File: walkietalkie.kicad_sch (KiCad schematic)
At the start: 7 parts, among them SW2 SW_Push, U2 NRF24L01_Breakout

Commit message: schematics done
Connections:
- net +3.3V: now also 1.VCC, Brd1.2 (VCC), U2.2 (VCC), U4.1 (3.3V)
- net SCL: now reaches Brd1.3 (SCL), U1.1 (SCL)
- net SCL: now also U3.5 (SCL)
- net BAT: now reaches U1.12 (BAT)
- net BAT: now also U3.1 (5V)
- net at U1.14 (3V3): no longer Brd1.2 (VCC)
- net GND: now reaches Brd1.1 (GND), U2.1 (GND)
- net GND: now also 1.GND, SW2.2, U1.28 (GND), U3.3 (G), U4.2 (GND); no longer U1.16 (GND)
- net CE: now reaches U1.17 (D13)
- net CE: now also U2.3 (CE)
- net CSN: now reaches U1.18 (D14)
- net CSN: now also U2.4 (~{CSN})
- net SDA: now reaches Brd1.4 (SDA), U1.2 (SDA)
- net SDA: now also U3.4 (SDA)
- net MIC_SD: now reaches U1.20 (D16)
- net MIC_SD: now also U4.5 (SD)
- net LRCK: now reaches U1.21 (D17)
- net LRCK: now also U3.9 (LRCK), U4.3 (WS)
- net BCLK: now reaches U1.22 (D18)
- net BCLK: now also U3.7 (BCK), U4.4 (SCK)
- net SCK: now reaches U1.23 (SCK)
- net SCK: now also U2.5 (SCK)
- net MO: now reaches U1.24 (MO)
- net MO: now also U2.6 (MOSI)
- net MI: now reaches U1.25 (MI)
- net MI: now also U2.7 (MISO)
- net ENC_SW: now reaches U1.4 (A2)
- net ENC_SW: now also 1.SW
- net NAU_MCLK: now reaches U1.5 (A6)
- net NAU_MCLK: now also U3.6 (MCLK)
- net NAU_DAT: now reaches U1.6 (A7)
- net NAU_DAT: now also U3.8 (DAT)
- net ENC_A: now reaches U1.7 (A8)
- net ENC_A: now also 1.CLK
- net PTT: now reaches U1.8 (A9)
- net PTT: now also SW2.1
- net ENC_B: now reaches U1.9 (A10)
- net ENC_B: now also 1.DT
- new net +3V3: U1.15 (3V3)
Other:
- moved on the sheet: 1, Brd1, U1, U3, U4

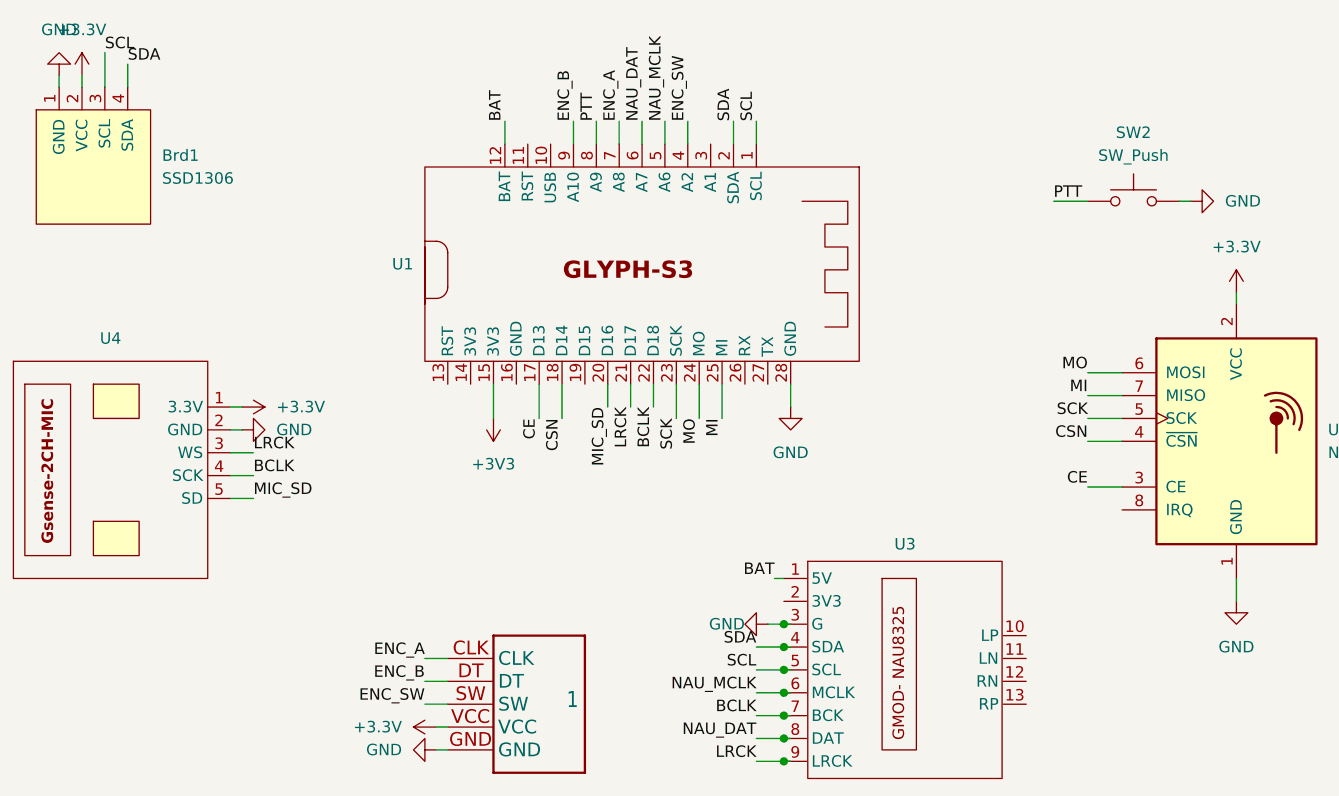
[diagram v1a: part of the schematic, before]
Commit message: assigning footprints done
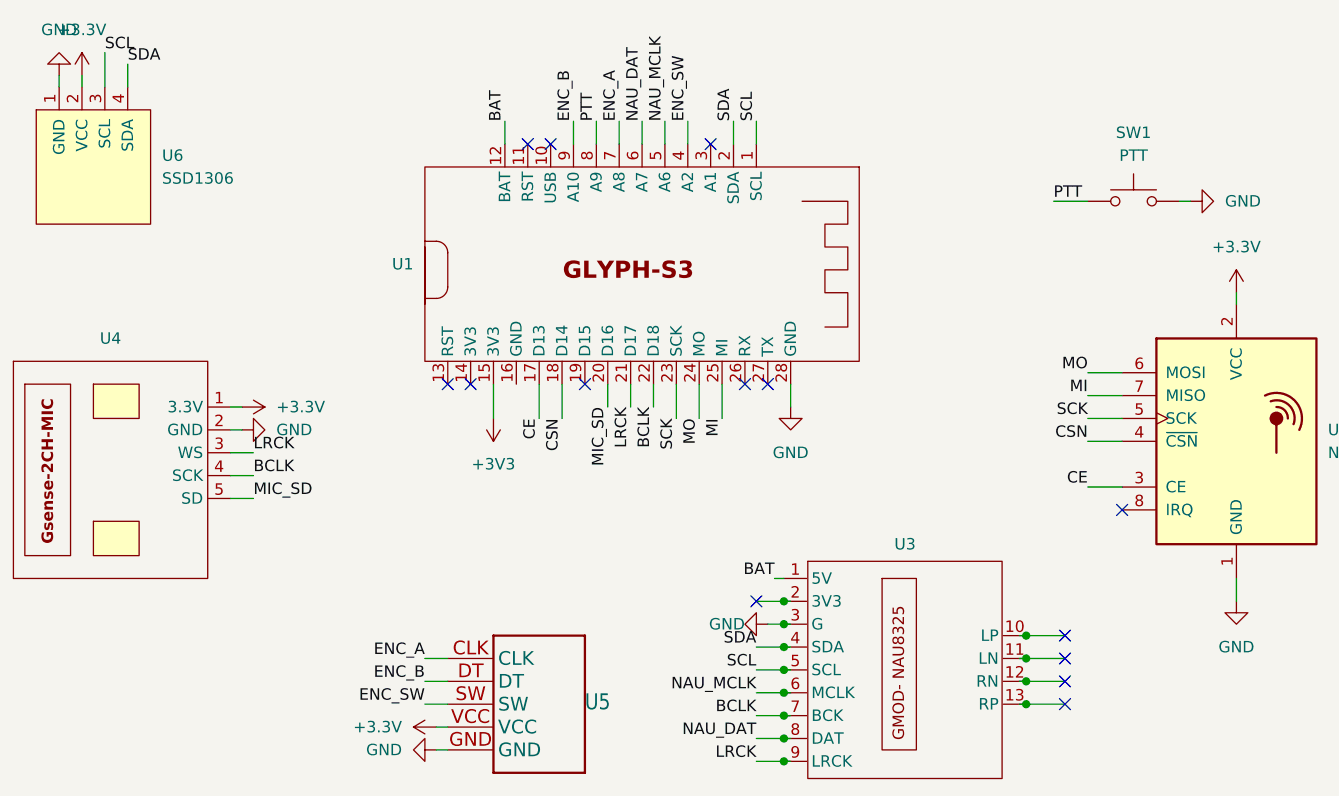
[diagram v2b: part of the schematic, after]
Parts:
- SW1: renamed from SW2; value SW_Push -> PTT; footprint (none) -> Button_Switch_THT:SW_SPST_Omron_B3F-315x_Angled
- U1: footprint GLYPHC6:GLYPH-C6 -> pcbcupid_footprint:glyph-s3
- U3: footprint Audiocodec_foot:Audio_codec -> pcbcupid_footprint:gmod-audio_codec
- U4: footprint (none) -> pcbcupid_footprint:gsense-microphone_2ch
- U5: renamed from 1; footprint KY-040:KY-040-PORT -> kicadfoots:KY-040-PORT
- U6: renamed from Brd1; footprint (none) -> kicadfoots:128x64OLED
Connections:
- no-connect marks 0 -> 14

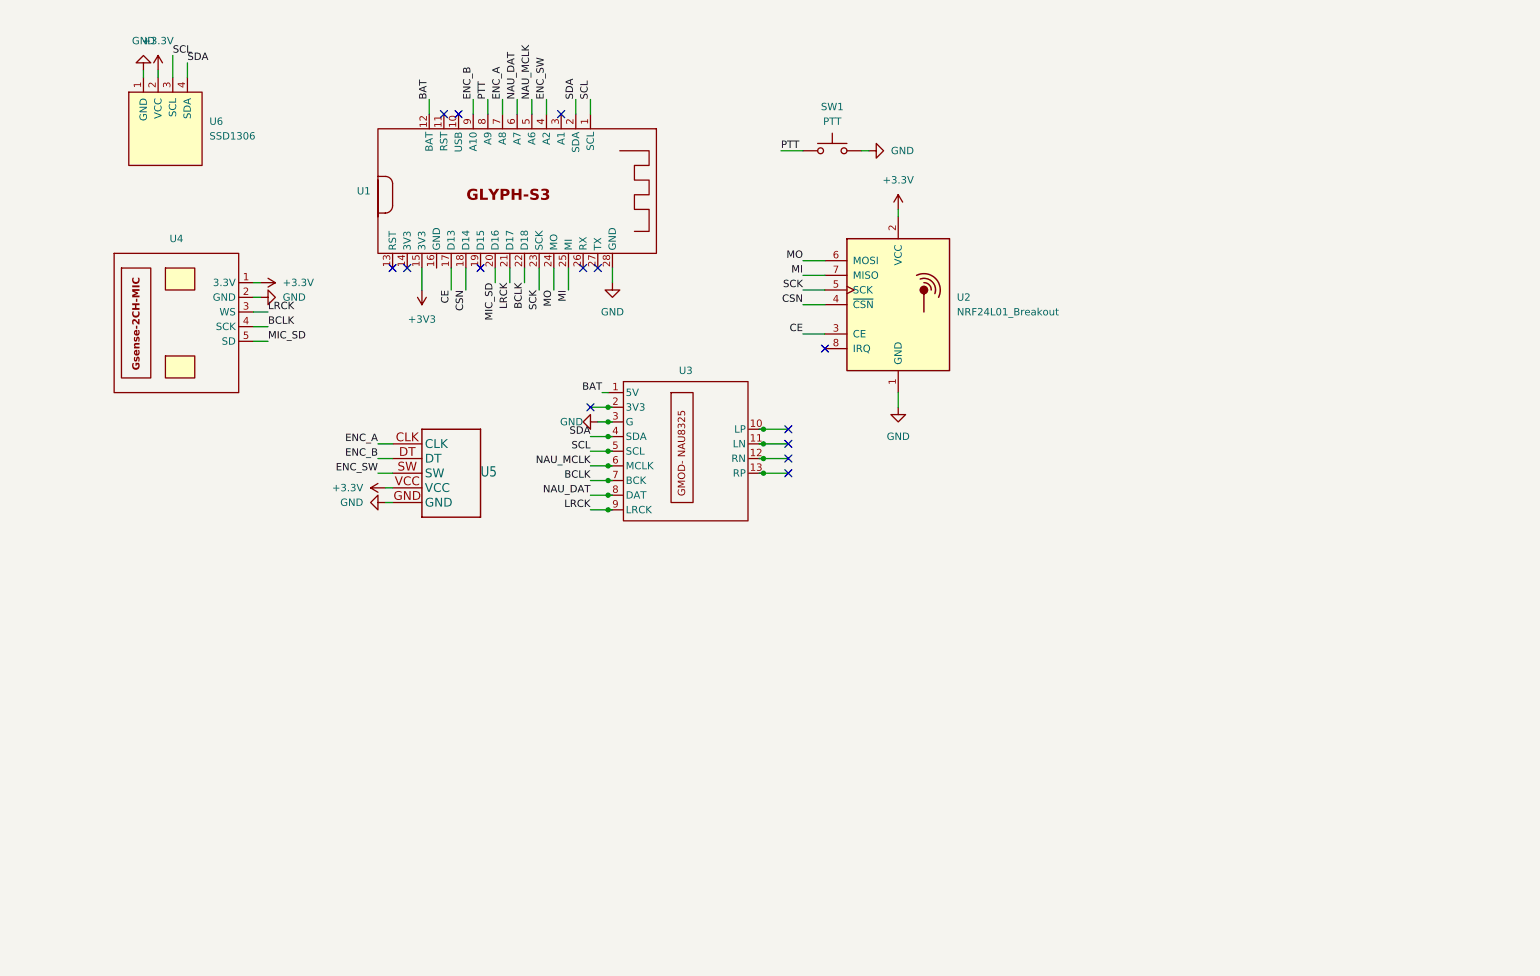
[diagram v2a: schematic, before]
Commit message: placements of the components are done, routing left
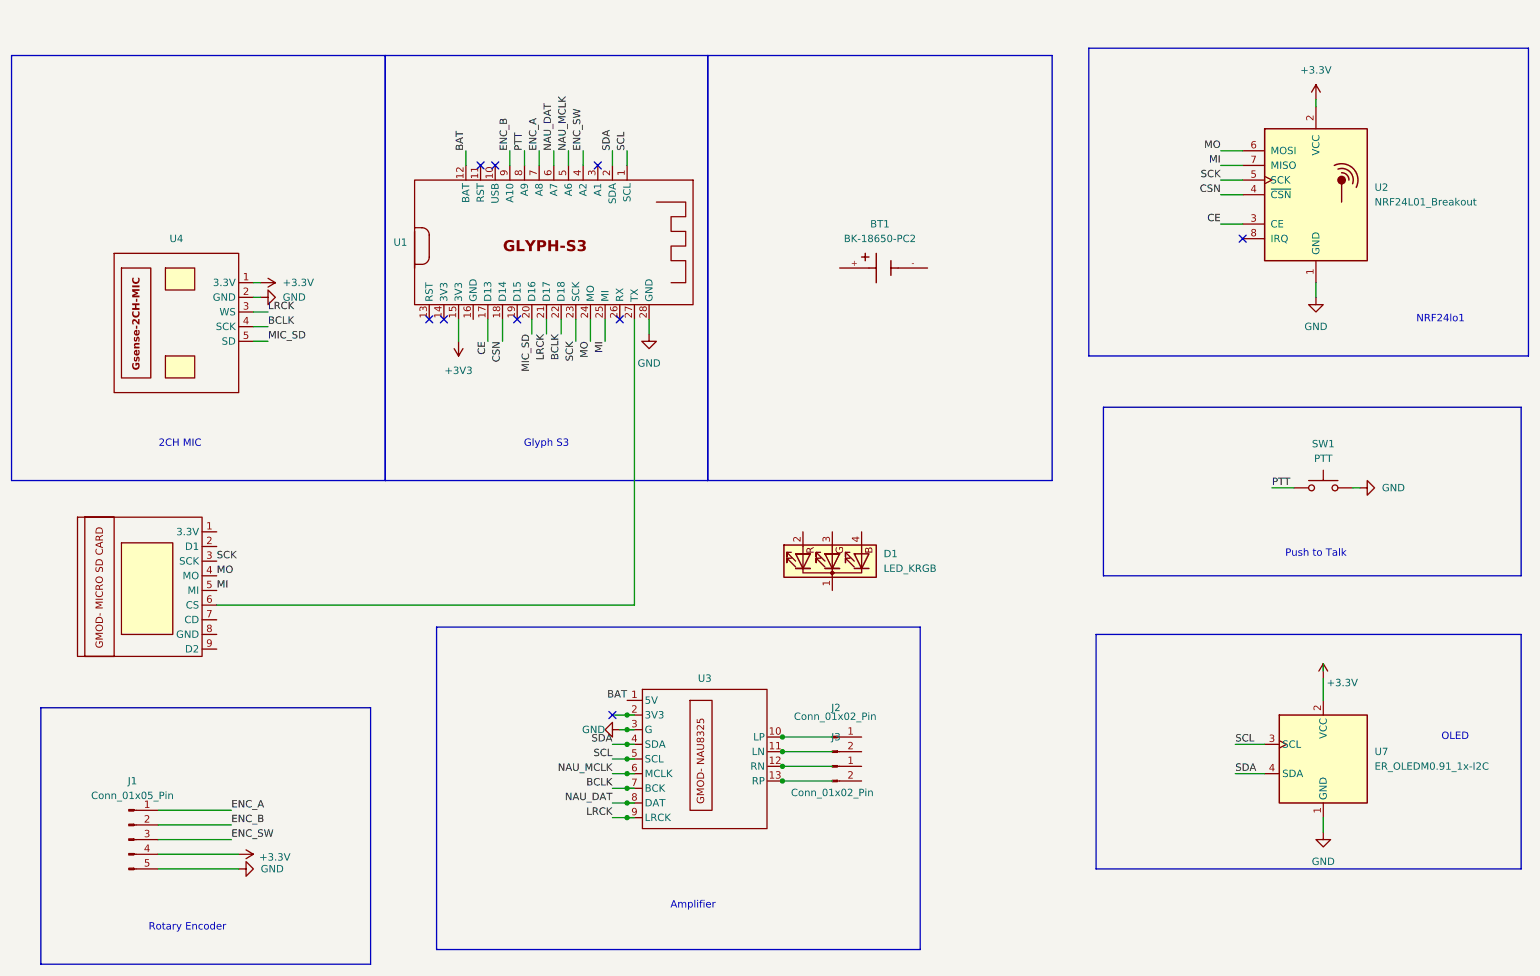
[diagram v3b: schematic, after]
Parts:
- removed U5: (no value), kicadfoots:KY-040-PORT, symbol KY-040:KY-040
- removed U6: SSD1306, kicadfoots:128x64OLED, symbol SSD1306-128x64_OLED:SSD1306
- added BT1: BK-18650-PC2, pcbcupid_footprint:BAT_BK-18650-PC2, symbol single:BK-18650-PC2
- added D1: LED_KRGB, symbol Device:LED_KRGB
- added J1: Conn_01x05_Pin, Connector_PinHeader_1.27mm:PinHeader_1x05_P1.27mm_Horizontal, symbol Connector:Conn_01x05_Pin
- added J2, J3: Conn_01x02_Pin, symbol Connector:Conn_01x02_Pin
- added U5: (no value), pcbcupid_footprint:gmod-micro_sd, symbol single:GMOD- MICRO SD CARD
- added U7: ER_OLEDM0.91_1x-I2C, Display:ER_OLEDM0.91_1x-I2C, symbol Display_Graphic:ER_OLEDM0.91_1x-I2C
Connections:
- net +3.3V: now also J1.4 (Pin_4), U7.2 (VCC)
- net ENC_A: now also J1.1 (Pin_1)
- net ENC_B: now also J1.2 (Pin_2)
- net ENC_SW: now also J1.3 (Pin_3)
- net GND: now also J1.5 (Pin_5), U7.1 (GND)
- net MI: now also U5.5 (MI)
- net MO: now also U5.4 (MO)
- net SCK: now also U5.3 (SCK)
- net SCL: now also U7.3 (SCL)
- net SDA: now also U7.4 (SDA)
- net at U1.27 (TX): now also U5.6 (CS)
- no-connect marks 14 -> 9
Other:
- note added: "2CH MIC"
- note added: "Amplifier"
- note added: "Glyph S3"
- note added: "NRF24lo1"
- note added: "OLED"
- note added: "Push to Talk"
- note added: "Rotary Encoder"
- company: (none) -> PCB CUPID
- title: (none) -> TeleVox
- moved on the sheet: SW1, U1, U2, U3

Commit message: feat: finalize component placement, routing remaining
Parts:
- BT1: footprint pcbcupid_footprint:BAT_BK-18650-PC2 -> pcbcupidd_footprint:BatteryHolder_1042_1x18650
- D1: footprint (none) -> LED_THT:LED_D5.0mm-4_RGB
- J1: footprint Connector_PinHeader_1.27mm:PinHeader_1x05_P1.27mm_Horizontal -> Connector_PinHeader_2.54mm:PinHeader_1x05_P2.54mm_Vertical
- J2, J3: footprint (none) -> Connector_JST:JST_XH_S2B-XH-A_1x02_P2.50mm_Horizontal
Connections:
- no-connect marks 9 -> 12

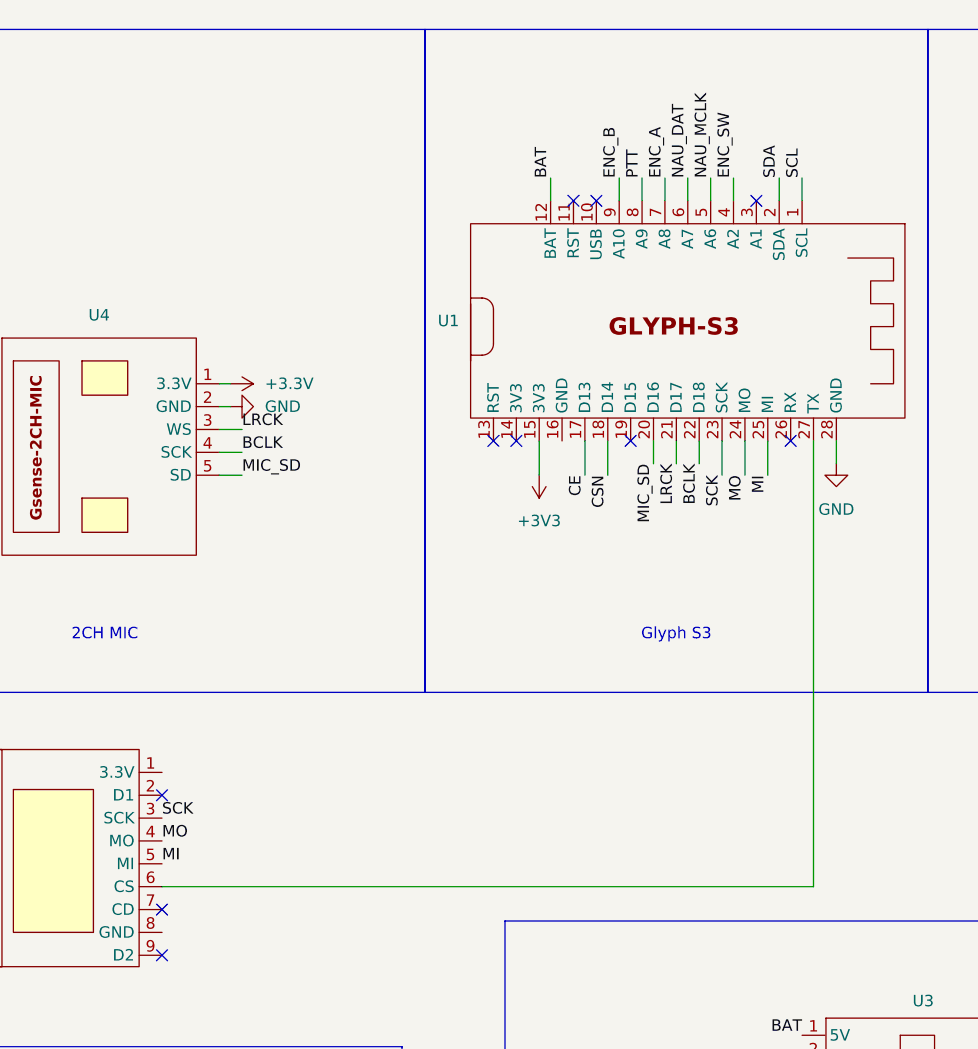
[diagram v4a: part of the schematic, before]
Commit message: feat: initial routing progress, fix 2ch mic footprint
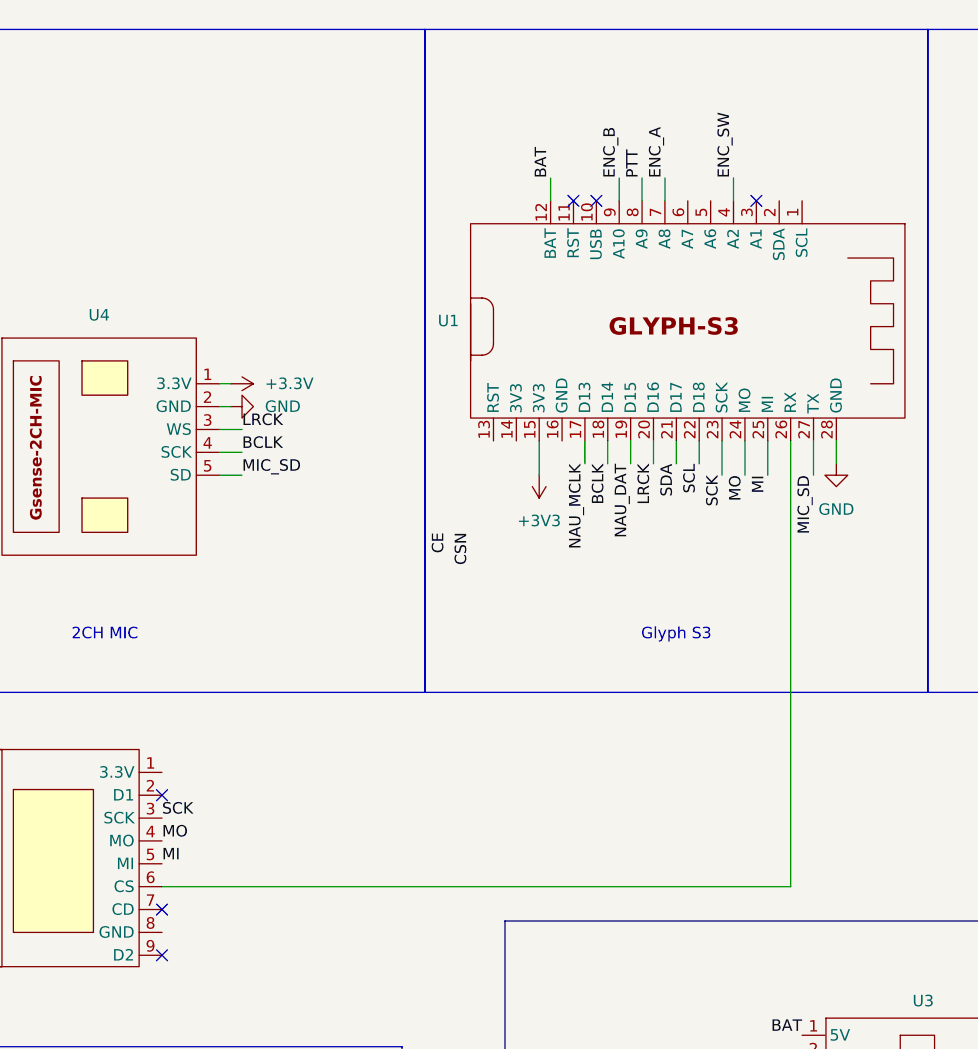
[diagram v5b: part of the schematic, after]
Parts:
- U4: footprint pcbcupid_footprint:gsense-microphone_2ch -> pcbcupidd_footprint:CH2 mic
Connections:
- net BCLK: now also U1.18 (D14); no longer U1.22 (D18)
- net CE: no longer U1.17 (D13)
- net CSN: no longer U1.18 (D14)
- net LRCK: now also U1.20 (D16); no longer U1.21 (D17)
- net MIC_SD: now also U1.27 (TX); no longer U1.20 (D16)
- net NAU_DAT: now also U1.19 (D15); no longer U1.6 (A7)
- net NAU_MCLK: now also U1.17 (D13); no longer U1.5 (A6)
- net SCL: now also U1.22 (D18); no longer U1.1 (SCL)
- net SDA: now also U1.21 (D17); no longer U1.2 (SDA)
- net at U1.26 (RX): now also U5.6 (CS)
- no-connect marks 12 -> 8
